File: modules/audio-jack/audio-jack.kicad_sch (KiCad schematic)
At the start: 6 parts, among them J1 SJ-43514-SMT-TR

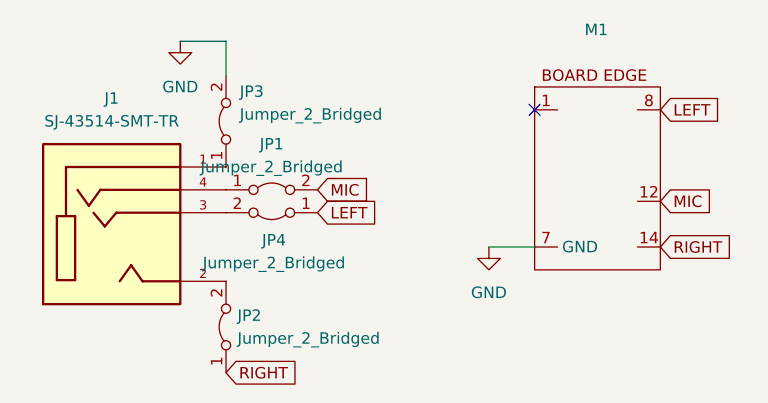
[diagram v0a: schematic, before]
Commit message: KiCad v9 adding new footprints
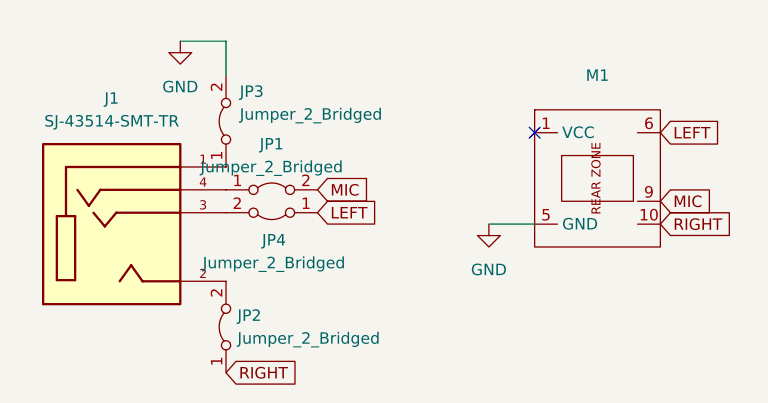
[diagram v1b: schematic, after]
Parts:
- J1: footprint CUI_SJ-43514-SMT-TR -> audio-jack:CUI_SJ-43514-SMT-TR
- M1: footprint MegaCastle:MegaCastle2x7-Module-I12.7x13.0-M8314-PANEL-NIBBLE -> MegaCastle:MegaCastle2x7-Module-I15.0x13.0-M8314-SPAREPAD; symbol MegaCastle:MegaCastle2x7-Module-I12.7x13.0-M8314-NOCUTOUT-EDGE -> MegaCastle:MegaCastle2x5-Module-I15.0x7.9-M8CC
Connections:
- net GND: now also M1.5 (GND); no longer M1.7 (GND)
- net LEFT: now also M1.6; no longer M1.8
- net MIC: now also M1.9; no longer M1.12
- net RIGHT: now also M1.10; no longer M1.14
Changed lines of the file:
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@@
 (kicad_sch
-	(version 20231120)
+	(version 20250114)
 	(generator "eeschema")
-	(generator_version "8.0")
+	(generator_version "9.0")
 	(paper "A4")
 	(no_connect
-		(at 114.3 45.72)
+		(at 114.3 48.26)
 	)
 	(wire
 		(pts
-			(xy 109.22 60.96) (xy 114.3 60.96)
+			(xy 109.22 58.42) (xy 114.3 58.42)
 		)
 		(stroke
@@
 	(global_label "LEFT"
 		(shape input)
-		(at 128.27 45.72 0)
+		(at 128.27 48.26 0)
 		(fields_autoplaced yes)
 		(effects
@@
 		)
 		(property "Intersheetrefs" "${INTERSHEET_REFS}"
-			(at 135.4885 45.72 0)
+			(at 135.4885 48.26 0)
 			(effects
 				(font
@@
 	(global_label "RIGHT"
 		(shape input)
-		(at 128.27 60.96 0)
+		(at 128.27 58.42 0)
 		(fields_autoplaced yes)
 		(effects
@@
 		)
 		(property "Intersheetrefs" "${INTERSHEET_REFS}"
-			(at 136.6981 60.96 0)
+			(at 136.6981 58.42 0)
 			(effects
 				(font
@@
 			)
 		)
-		(property "Footprint" "CUI_SJ-43514-SMT-TR"
+		(property "Footprint" "audio-jack:CUI_SJ-43514-SMT-TR"
 			(at 67.31 57.15 0)
 			(effects
@@
 	(symbol
 		(lib_id "power:GND")
-		(at 109.22 60.96 0)
+		(at 109.22 58.42 0)
 		(unit 1)
 		(exclude_from_sim no)
@@
 		(fields_autoplaced yes)
 		(property "Reference" "#PWR02"
-			(at 109.22 67.31 0)
+			(at 109.22 64.77 0)
 			(effects
 				(font
@@
 		)
 		(property "Value" "GND"
-			(at 109.22 66.04 0)
+			(at 109.22 63.5 0)
 			(effects
 				(font
@@
 		)
 		(property "Footprint" ""
-			(at 109.22 60.96 0)
+			(at 109.22 58.42 0)
 			(effects
 				(font
@@
 		)
 		(property "Datasheet" ""
-			(at 109.22 60.96 0)
+			(at 109.22 58.42 0)
 			(effects
 				(font
@@
 		)
 		(property "Description" "Power symbol creates a global label with name \"GND\" , ground"
-			(at 109.22 60.96 0)
+			(at 109.22 58.42 0)
 			(effects
 				(font
@@
 	)
 	(symbol
-		(lib_id "MegaCastle:MegaCastle2x7-Module-I12.7x13.0-M8314-NOCUTOUT-EDGE")
+		(lib_id "MegaCastle:MegaCastle2x5-Module-I15.0x7.9-M8CC")
 		(at 120.65 53.34 0)
 		(unit 1)
@@
 		(fields_autoplaced yes)
 		(property "Reference" "M1"
-			(at 121.1538 36.83 0)
+			(at 121.285 41.91 0)
 			(effects
 				(font
@@
 		)
 		(property "Value" "~"
-			(at 121.1538 39.37 0)
-			(effects
-				(font
-					(size 1.27 1.27)
-				)
-			)
-		)
-		(property "Footprint" "MegaCastle:MegaCastle2x7-Module-I12.7x13.0-M8314-PANEL-NIBBLE"
-			(at 120.65 68.58 0)
+			(at 121.285 44.45 0)
+			(effects
+				(font
+					(size 1.27 1.27)
+				)
+			)
+		)
+		(property "Footprint" "MegaCastle:MegaCastle2x7-Module-I15.0x13.0-M8314-SPAREPAD"
+			(at 120.65 66.04 0)
 			(effects
 				(font
@@
 			)
 		)
-		(property "Description" "Generated using footprint-gen .. 12.7 11.5 5 2"
+		(property "Description" "Generated using footprint-gen ../ 15 15 5 M8CC"
 			(at 120.65 53.34 0)
 			(effects
@@
 			)
 		)
-		(pin "8"
-		)
-		(pin "12"
+		(pin "6"
+		)
+		(pin "5"
 		)
 		(pin "1"
 		)
-		(pin "14"
-		)
-		(pin "7"
+		(pin "9"
+		)
+		(pin "10"
 		)
 		(instances
@@
 		)
 	)
+	(embedded_fonts no)
 )
